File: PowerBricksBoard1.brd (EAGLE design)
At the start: 76.2 x 50.8 mm, 16 parts

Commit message: brick update
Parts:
- H1, H2, H3, H4: value STAND-OFF -> 6-32-HOLE; device SparkFun-Hardware:STAND-OFF -> Mounting Holes:6-32-HOLE
- moved H2 80.7 mm to (3.81, 3.81), turned to 0 degrees
- moved H3 68.4 mm to (72.4, 3.81), turned to 0 degrees
- moved H4 43.5 mm to (72.4, 47.0), turned to 0 degrees
- moved H1 0.19 mm to (3.81, 47.0), flipped to the bottom, turned to 0 degrees
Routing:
- net 12_GND: vias 21 -> 11
- net 12V: vias 20 -> 10

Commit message: test
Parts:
- removed U$6: BRICKBOARD_TSW_14X2, Dist_to_Brickboard_Connector_brick:BRICKBOARD_TSW_14X2
- added U$2: BRICK2DIST, Brick_Dist_Connector:BRICK2DIST
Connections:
- net 12V: now also U$2.2@1, U$2.2@10, U$2.2@11, U$2.2@12, U$2.2@13, U$2.2@14, U$2.2@15, U$2.2@16, U$2.2@2, U$2.2@3, U$2.2@4, U$2.2@5, U$2.2@6, U$2.2@7, U$2.2@8, U$2.2@9; no longer U$6.45, U$6.46, U$6.47, U$6.48, U$6.49, U$6.50, U$6.51, U$6.52, U$6.53, U$6.54, U$6.55, U$6.56
- net 12_GND: now also U$2.4@1, U$2.4@10, U$2.4@11, U$2.4@12, U$2.4@13, U$2.4@14, U$2.4@15, U$2.4@16, U$2.4@2, U$2.4@3, U$2.4@4, U$2.4@5, U$2.4@6, U$2.4@7, U$2.4@8, U$2.4@9; no longer U$6.29, U$6.30, U$6.31, U$6.32, U$6.33, U$6.34, U$6.35, U$6.36, U$6.37, U$6.38, U$6.39, U$6.40
- net 48V: now also U$2.1@1, U$2.1@10, U$2.1@2, U$2.1@3, U$2.1@4, U$2.1@5, U$2.1@6, U$2.1@7, U$2.1@8, U$2.1@9; no longer U$6.15, U$6.16, U$6.17, U$6.18, U$6.19, U$6.20, U$6.21, U$6.22, U$6.23, U$6.24, U$6.25, U$6.26, U$6.27, U$6.28
- net 48_GND: now also U$2.3@1, U$2.3@10, U$2.3@2, U$2.3@3, U$2.3@4, U$2.3@5, U$2.3@6, U$2.3@7, U$2.3@8, U$2.3@9; no longer U$6.10, U$6.11, U$6.12, U$6.13, U$6.14, U$6.3, U$6.4, U$6.5, U$6.6, U$6.7, U$6.8, U$6.9
- net ALERT: now also U$2.D; no longer U$6.43
- net CLK: now also U$2.C; no longer U$6.44
- net DATA: now also U$2.E; no longer U$6.42
- net ON/OFF: now also U$2.A, U$2.B; no longer U$6.1
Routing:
- net ON/OFF: track 137.9 -> 128.8 mm
- net ALERT: track 13.5 -> 4.78 mm
- net CLK: track 16.0 -> 14.2 mm
- net DATA: track 15.9 -> 14.2 mm
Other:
- board text added: "ADDR1 = R3 Resistor ADDR0 = R4 Resistor Octal Address = 8*ADDR1 + ADDR0 0-12 and 40, 44, 45, and 55 address can’t be used (decimal)"
- board text removed: "ADDR1 = R3 Resistor ADDR0 = R4 Resistor Octal Address = 8*ADDR1 + ADDR0"

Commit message: Ready for design review
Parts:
- moved H1 81.0 mm to (72.4, 3.81), flipped to the top
- moved H4 68.6 mm to (3.81, 47.0)
- moved U$2 53.8 mm to (41.9, 25.4)
- moved H3 43.2 mm to (72.4, 47.0)
- moved R2 27.5 mm to (24.1, 48.3), turned to 180 degrees
- moved D2 26.6 mm to (27.9, 48.3), turned to 0 degrees
- moved R1 23.5 mm to (73.3, 18.2), flipped to the bottom
- moved D1 22.6 mm to (52.1, 48.3), turned to 180 degrees
- moved C3 17.8 mm to (24.1, 24.1)
- moved C1 6.55 mm to (24.1, 24.1), flipped to the bottom
- moved R5 1.60 mm to (62.2, 24.1)
- moved R3 1.41 mm to (72.1, 24.1)
- moved U$1 1.27 mm to (15.2, 16.5)
- moved C2 1.27 mm to (6.35, 24.1)
- moved R4 1.27 mm to (74.4, 24.1)
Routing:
- net ALERT: track 4.78 -> 49.4 mm
- net N$1: track 1.32 -> 45.3 mm, vias 0 -> 1
- net 48V: track 0.00 -> 42.7 mm, vias 26 -> 0
- net CLK: track 14.2 -> 55.5 mm
- net ON/OFF: track 128.8 -> 98.8 mm
- net DATA: track 14.2 -> 43.8 mm
- net 48_GND: track 0.00 -> 10.1 mm, vias 39 -> 0
- net 12_GND: track 1.79 -> 10.1 mm, vias 11 -> 0
- net DGND: track 8.04 -> 7.15 mm
- net N$2: track 1.23 -> 2.08 mm
- net N$3: track 5.62 -> 4.86 mm
- net 12V: track 6.83 -> 7.57 mm, vias 10 -> 0
- net N$4: track 8.38 -> 8.89 mm
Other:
- board text removed: "ADDR1 = R3 Resistor ADDR0 = R4 Resistor Octal Address = 8*ADDR1 + ADDR0 0-12 and 40, 44, 45, and 55 address can’t be used (decimal)"
- board text removed: "Octal digit -> Resistor(Kohm) _________ 0 | 10 1 | 15.4 2 | 23.7 3 | 36.5 4 | 54.9 5 | 84.5 6 | 130 7 | 200"

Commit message: final
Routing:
- net 48_GND: vias 0 -> 9
- net 48V: vias 0 -> 9
- net 12_GND: vias 0 -> 11
- net 12V: vias 0 -> 10
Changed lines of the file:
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@@
 <vertex x="-1.27" y="19.05"/>
 </polygon>
+<via x="2.54" y="20.32" extent="1-16" drill="0.35"/>
+<via x="11.43" y="20.32" extent="1-16" drill="0.35"/>
+<via x="6.35" y="16.51" extent="1-16" drill="0.35"/>
+<via x="20.32" y="20.32" extent="1-16" drill="0.35"/>
+<via x="27.94" y="20.32" extent="1-16" drill="0.35"/>
+<via x="24.13" y="16.51" extent="1-16" drill="0.35"/>
+<via x="3.81" y="10.16" extent="1-16" drill="0.35"/>
+<via x="10.16" y="3.81" extent="1-16" drill="0.35"/>
+<via x="21.59" y="3.81" extent="1-16" drill="0.35"/>
 </signal>
 <signal name="48_GND">
@@
 <vertex x="2.032" y="25.908"/>
 </polygon>
+<via x="21.59" y="27.94" extent="1-16" drill="0.35"/>
+<via x="27.178" y="27.94" extent="1-16" drill="0.35"/>
+<via x="24.638" y="34.29" extent="1-16" drill="0.35"/>
+<via x="3.048" y="27.94" extent="1-16" drill="0.35"/>
+<via x="10.668" y="27.94" extent="1-16" drill="0.35"/>
+<via x="6.858" y="33.02" extent="1-16" drill="0.35"/>
+<via x="6.858" y="39.37" extent="1-16" drill="0.35"/>
+<via x="14.478" y="45.72" extent="1-16" drill="0.35"/>
+<via x="22.606" y="45.593" extent="1-16" drill="0.35"/>
 </signal>
 <signal name="12V">
@@
 <wire x1="73.279" y1="17.311" x2="72.478" y2="16.51" width="0.254" layer="16"/>
 <wire x1="72.478" y1="16.51" x2="66.04" y2="16.51" width="0.254" layer="16"/>
+<via x="33.02" y="21.59" extent="1-16" drill="0.35"/>
+<via x="46.99" y="21.59" extent="1-16" drill="0.35"/>
+<via x="59.69" y="21.59" extent="1-16" drill="0.35"/>
+<via x="53.34" y="15.24" extent="1-16" drill="0.35"/>
+<via x="36.83" y="15.24" extent="1-16" drill="0.35"/>
+<via x="29.21" y="3.81" extent="1-16" drill="0.35"/>
+<via x="53.34" y="3.81" extent="1-16" drill="0.35"/>
+<via x="59.69" y="8.89" extent="1-16" drill="0.35"/>
+<via x="66.04" y="3.81" extent="1-16" drill="0.35"/>
+<via x="66.04" y="11.43" extent="1-16" drill="0.35"/>
 </signal>
 <signal name="ON/OFF">
@@
 <vertex x="26.289" y="43.815"/>
 </polygon>
+<via x="31.75" y="27.94" extent="1-16" drill="0.35"/>
+<via x="46.99" y="27.94" extent="1-16" drill="0.35"/>
+<via x="59.69" y="27.94" extent="1-16" drill="0.35"/>
+<via x="66.04" y="38.1" extent="1-16" drill="0.35"/>
+<via x="63.5" y="43.18" extent="1-16" drill="0.35"/>
+<via x="54.61" y="43.18" extent="1-16" drill="0.35"/>
+<via x="48.26" y="44.45" extent="1-16" drill="0.35"/>
+<via x="50.8" y="41.91" extent="1-16" drill="0.35"/>
+<via x="57.15" y="35.56" extent="1-16" drill="0.35"/>
+<via x="39.37" y="34.29" extent="1-16" drill="0.35"/>
+<via x="30.48" y="44.45" extent="1-16" drill="0.35"/>
 </signal>
 <signal name="ALERT">

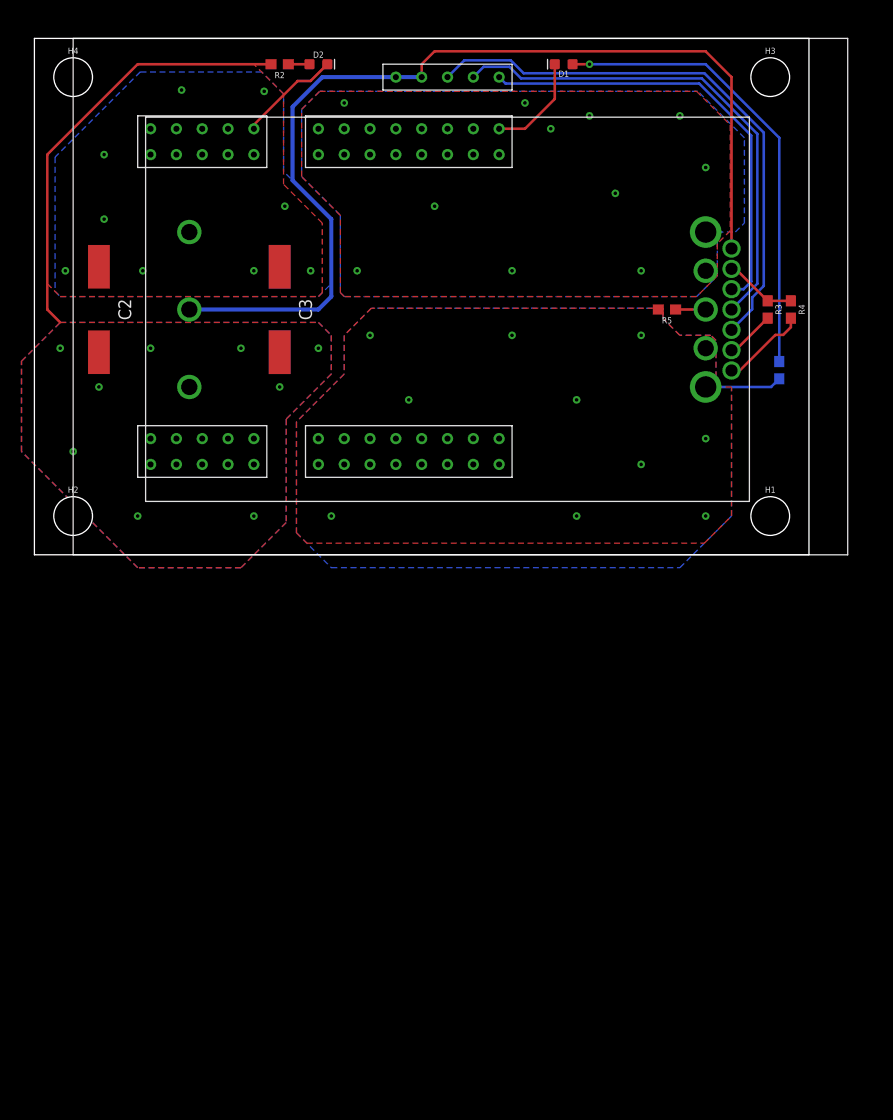
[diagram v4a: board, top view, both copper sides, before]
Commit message: cad placement for tyler (routing not done)
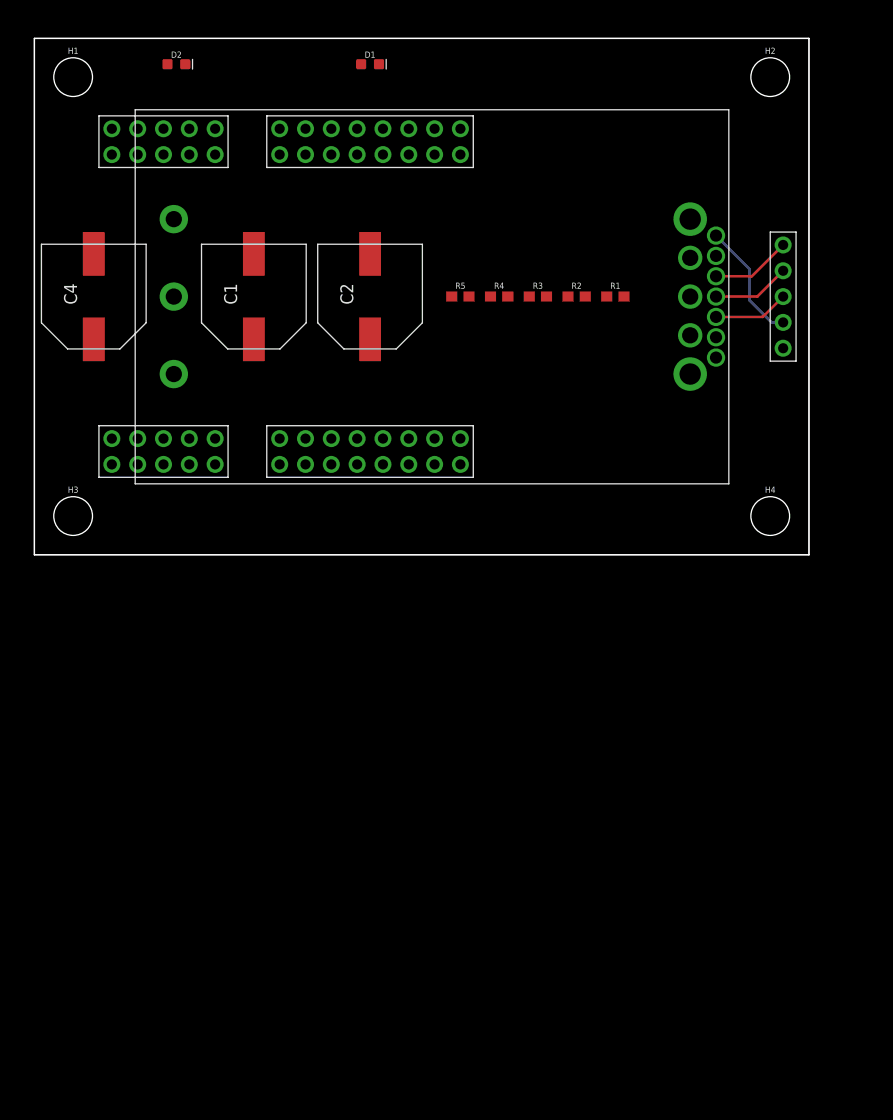
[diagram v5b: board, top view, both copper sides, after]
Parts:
- removed C3: UCM1H331MNL1GS, UCM1H331MNL1GS:CAPAE1030X1050N
- removed U$1: Q48SC12050NRDH, Q48SC12050NRDH:Q48SC12050NRDH
- added C4: 330uF, brick-capacitor-UCM1H331MNL1GS:CAPAE1030X1050N
- added U$3: BRICK2DIST_C, Brick_Dist_Connector:BRICK2DIST_C
- C1, C2: value UCM1H331MNL1GS -> 330uF; device UCM1H331MNL1GS:CAPAE1030X1050N -> brick-capacitor-UCM1H331MNL1GS:CAPAE1030X1050N
- U$2: value BRICK2DIST -> Q48SC12050NRDH; device Brick_Dist_Connector:BRICK2DIST -> Delta Power Bricks - Q48SC12050NRDH:Q48SC12050NRDH
- moved H1 81.0 mm to (3.81, 47.0)
- moved H2 81.0 mm to (72.4, 47.0)
- moved H3 81.0 mm to (3.81, 3.81)
- moved H4 81.0 mm to (72.4, 3.81)
- moved R2 37.1 mm to (53.3, 25.4), turned to 0 degrees
- moved U$2 29.2 mm to (13.7, 17.8)
- moved R4 28.7 mm to (45.7, 25.4), turned to 0 degrees
- moved C2 26.7 mm to (33.0, 25.4)
- moved R3 22.6 mm to (49.5, 25.4), turned to 0 degrees
- moved R5 20.4 mm to (41.9, 25.4), turned to 0 degrees
- moved D1 19.0 mm to (33.0, 48.3), turned to 0 degrees
- moved R1 17.7 mm to (57.1, 25.4), flipped to the top, turned to 0 degrees
- moved D2 14.0 mm to (14.0, 48.3)
- moved C1 2.84 mm to (21.6, 25.4), flipped to the top
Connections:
- removed net ON/OFF: U$1.C2, U$1.ON/OFF, U$2.A, U$2.B
- new net C2: U$2.10, U$2.2, U$3.A, U$3.B
- net 12V: now also U$2.8, U$2.9, U$3.2@1, U$3.2@10, U$3.2@11, U$3.2@12, U$3.2@13, U$3.2@14, U$3.2@15, U$3.2@16, U$3.2@2, U$3.2@3, U$3.2@4, U$3.2@5, U$3.2@6, U$3.2@7, U$3.2@8, U$3.2@9; no longer U$1.12V, U$1.SENSE+, U$2.2@1, U$2.2@10, U$2.2@11, U$2.2@12, U$2.2@13, U$2.2@14, U$2.2@15, U$2.2@16, U$2.2@2, U$2.2@3, U$2.2@4, U$2.2@5, U$2.2@6, U$2.2@7, U$2.2@8, U$2.2@9
- net 12_GND: now also U$2.5, U$2.6, U$3.4@1, U$3.4@10, U$3.4@11, U$3.4@12, U$3.4@13, U$3.4@14, U$3.4@15, U$3.4@16, U$3.4@2, U$3.4@3, U$3.4@4, U$3.4@5, U$3.4@6, U$3.4@7, U$3.4@8, U$3.4@9; no longer U$1.12V_GND, U$1.SENSE-, U$2.4@1, U$2.4@10, U$2.4@11, U$2.4@12, U$2.4@13, U$2.4@14, U$2.4@15, U$2.4@16, U$2.4@2, U$2.4@3, U$2.4@4, U$2.4@5, U$2.4@6, U$2.4@7, U$2.4@8, U$2.4@9
- net 48V: now also C1.+, C2.+, C4.+, U$2.1, U$3.1@1, U$3.1@10, U$3.1@2, U$3.1@3, U$3.1@4, U$3.1@5, U$3.1@6, U$3.1@7, U$3.1@8, U$3.1@9; no longer C1.1, C2.1, C3.1, U$1.48V, U$2.1@1, U$2.1@10, U$2.1@2, U$2.1@3, U$2.1@4, U$2.1@5, U$2.1@6, U$2.1@7, U$2.1@8, U$2.1@9
- net 48_GND: now also C1.-, C2.-, C4.-, U$2.4, U$3.3@1, U$3.3@10, U$3.3@2, U$3.3@3, U$3.3@4, U$3.3@5, U$3.3@6, U$3.3@7, U$3.3@8, U$3.3@9; no longer C1.2, C2.2, C3.2, U$1.48V_GND, U$2.3@1, U$2.3@10, U$2.3@2, U$2.3@3, U$2.3@4, U$2.3@5, U$2.3@6, U$2.3@7, U$2.3@8, U$2.3@9
- net ALERT: now also U$2.13, U$3.D; no longer U$1.SMBALERT, U$2.D
- net CLK: now also U$2.14, U$3.C; no longer U$1.PMBCLK, U$2.C
- net DATA: now also U$2.12, U$3.E; no longer U$1.PMBDATA, U$2.E
- net DGND: now also U$2.11; no longer U$1.DGND
- net N$3: now also U$2.15; no longer U$1.ADDR1
- net N$4: now also U$2.16; no longer U$1.ADDR0
- net N$5: now also U$2.7; no longer U$1.TRIM
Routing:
- net ON/OFF: track 98.8 -> 0.00 mm
- net CLK: track 55.5 -> 7.43 mm
- net N$1: track 45.3 -> 0.00 mm, vias 1 -> 0
- net 48V: track 42.7 -> 0.00 mm, vias 9 -> 0
- net ALERT: track 49.4 -> 7.66 mm
- net DATA: track 43.8 -> 7.88 mm
- net C2: track 0.00 -> 11.9 mm
- net 12_GND: track 10.1 -> 0.00 mm, vias 11 -> 0
- net 48_GND: track 10.1 -> 0.00 mm, vias 9 -> 0
- net N$4: track 8.89 -> 0.00 mm
- net 12V: track 7.57 -> 0.00 mm, vias 10 -> 0
- net DGND: track 7.15 -> 0.00 mm
- net N$3: track 4.86 -> 0.00 mm
- net N$5: track 2.96 -> 0.00 mm
- net N$2: track 2.08 -> 0.00 mm
- removed copper zone on layer 1, net 12V
- removed copper zone on layer 16, net 12V
- removed copper zone on layer 1, net 12_GND
- removed copper zone on layer 16, net 12_GND
- removed copper zone on layer 1, net 48V
- removed copper zone on layer 16, net 48V
- removed copper zone on layer 1, net 48_GND
- removed copper zone on layer 16, net 48_GND

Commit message: Owo
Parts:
- moved R2 48.2 mm to (11.4, 49.3), turned to 180 degrees
- moved D1 43.0 mm to (74.7, 37.5), turned to 90 degrees
- moved R1 19.7 mm to (74.7, 34.3), turned to 270 degrees
- moved R5 19.2 mm to (61.0, 22.7), turned to 270 degrees
- moved R4 12.8 mm to (58.4, 26.7), turned to 270 degrees
- moved R3 11.5 mm to (61.0, 26.7), turned to 270 degrees
- moved D2 1.20 mm to (14.6, 49.3)
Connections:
- new net ON/OFF: U$2.2, U$3.B
- net C2: no longer U$2.2, U$3.B
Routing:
- net ON/OFF: track 0.00 -> 126.2 mm
- net 48V: track 0.00 -> 31.5 mm, vias 0 -> 14
- net 12V: track 0.00 -> 17.4 mm, vias 0 -> 21
- net N$4: track 0.00 -> 13.1 mm
- net DGND: track 0.00 -> 9.41 mm
- net N$3: track 0.00 -> 7.93 mm
- net N$5: track 0.00 -> 4.41 mm, vias 0 -> 1
- net C2: track 11.9 -> 14.2 mm
- net 48_GND: track 0.00 -> 2.04 mm, vias 0 -> 16
- net N$2: track 0.00 -> 1.45 mm
- net N$1: track 0.00 -> 1.45 mm
- net 12_GND: track 0.00 -> 1.26 mm, vias 0 -> 15
- added copper zone on layer 1, net 12V
- added copper zone on layer 16, net 12V
- added copper zone on layer 1, net 12_GND
- added copper zone on layer 16, net 12_GND
- added copper zone on layer 1, net 48V
- added copper zone on layer 16, net 48V
- added copper zone on layer 1, net 48_GND
- added copper zone on layer 16, net 48_GND
